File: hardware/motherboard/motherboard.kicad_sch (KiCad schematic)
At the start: 80 parts, among them J1 JST-VH, J2 USB C 2.0, J3 JST-VH, J4 JST-PH, J5 IMU Connector, Q1 TSM7P06CP_ROG, Q2 TSM7P06CP_ROG, SW10 B, SW11 X, SW12 Y, SW13 Start, SW14 Select, SW2 Reset, SW3 A, SW4 B, SW5 LB, SW6 RB, SW7 X, SW8 Y, SW9 A, U1 ESP32-S3-WROOM-1, U2 TPS75533KTTRG3, U3 TLV75709PDBV, U4 MCP73831-2-OT

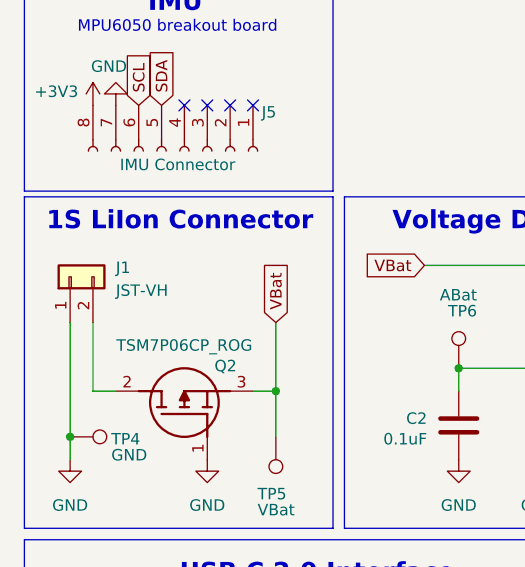
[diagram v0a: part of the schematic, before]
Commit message: Cont. Motherboard Layout
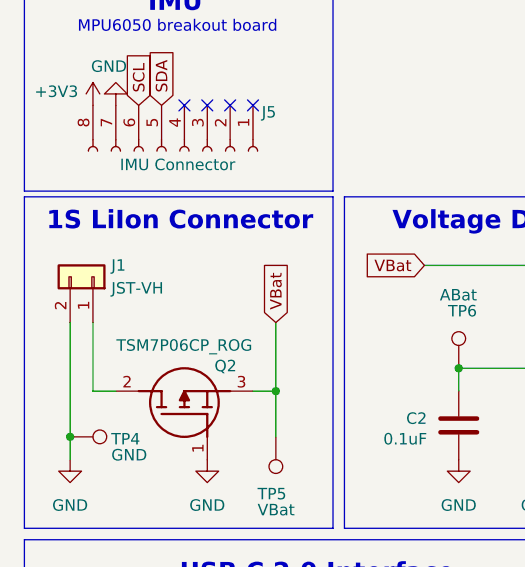
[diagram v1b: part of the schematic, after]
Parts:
- C1, C10, C5, C6, C7, C8: footprint (none) -> Capacitor_SMD:C_1206_3216Metric_Pad1.33x1.80mm_HandSolder
- C12, C13, C14, C15, C16, C17, C18, C19, C20, C21, C22, C23: footprint Capacitor_SMD:C_0201_0603Metric -> Capacitor_SMD:C_1206_3216Metric_Pad1.33x1.80mm_HandSolder
- C2, C4: footprint (none) -> Capacitor_SMD:C_0805_2012Metric_Pad1.18x1.45mm_HandSolder
- C3: footprint (none) -> Capacitor_Tantalum_SMD:CP_EIA-7343-31_Kemet-D
- R1, R10, R2, R23, R24, R25, R3, R4, R5, R6, R7, R9: footprint (none) -> Resistor_SMD:R_0805_2012Metric_Pad1.20x1.40mm_HandSolder
- R11, R12, R13, R14, R15, R16, R17, R18, R19, R20, R21, R22, R8: footprint Resistor_SMD:R_0603_1608Metric -> Resistor_SMD:R_0805_2012Metric_Pad1.20x1.40mm_HandSolder
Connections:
- net GND: now also J1.2 (Pin_2); no longer J1.1 (Pin_1)
- net at Q2.2 (D): now also J1.1 (Pin_1); no longer J1.2 (Pin_2)
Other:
- moved on the sheet: J1

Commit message: Routing 💀
Layout and routing. Used 3v3 plane to route some power traces.

Also added full size joystick model and footprint and schematic.
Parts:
- removed JY1: B10k, esp32_handheld:Low_Profile_Joystick, symbol esp32_handheld:Low_Profile_Joystick
- added C23: 1uF, Capacitor_SMD:C_0805_2012Metric_Pad1.18x1.45mm_HandSolder, symbol Device:C
- added R26: 10k, Resistor_SMD:R_0805_2012Metric_Pad1.20x1.40mm_HandSolder, symbol Device:R_US
- added U5: COM-09032, esp32_handheld:XDCR_COM-09032, symbol esp32_handheld:COM-09032
- C1: renamed from C12; footprint Capacitor_SMD:C_1206_3216Metric_Pad1.33x1.80mm_HandSolder -> Capacitor_SMD:C_0805_2012Metric_Pad1.18x1.45mm_HandSolder
- C10: renamed from C19; footprint Capacitor_SMD:C_1206_3216Metric_Pad1.33x1.80mm_HandSolder -> Capacitor_SMD:C_0805_2012Metric_Pad1.18x1.45mm_HandSolder
- C11: renamed from C20; footprint Capacitor_SMD:C_1206_3216Metric_Pad1.33x1.80mm_HandSolder -> Capacitor_SMD:C_0805_2012Metric_Pad1.18x1.45mm_HandSolder
- C12: renamed from C21; footprint Capacitor_SMD:C_1206_3216Metric_Pad1.33x1.80mm_HandSolder -> Capacitor_SMD:C_0805_2012Metric_Pad1.18x1.45mm_HandSolder
- C14: renamed from C10; footprint Capacitor_SMD:C_1206_3216Metric_Pad1.33x1.80mm_HandSolder -> Capacitor_SMD:C_0805_2012Metric_Pad1.18x1.45mm_HandSolder
- C15: renamed from C8; footprint Capacitor_SMD:C_1206_3216Metric_Pad1.33x1.80mm_HandSolder -> Capacitor_SMD:C_0805_2012Metric_Pad1.18x1.45mm_HandSolder
- C17: renamed from C7; footprint Capacitor_SMD:C_1206_3216Metric_Pad1.33x1.80mm_HandSolder -> Capacitor_SMD:C_0805_2012Metric_Pad1.18x1.45mm_HandSolder
- C18: renamed from C6; footprint Capacitor_SMD:C_1206_3216Metric_Pad1.33x1.80mm_HandSolder -> Capacitor_SMD:C_0805_2012Metric_Pad1.18x1.45mm_HandSolder
- C19: renamed from C1; footprint Capacitor_SMD:C_1206_3216Metric_Pad1.33x1.80mm_HandSolder -> Capacitor_SMD:C_0805_2012Metric_Pad1.18x1.45mm_HandSolder
- C2: renamed from C13; footprint Capacitor_SMD:C_1206_3216Metric_Pad1.33x1.80mm_HandSolder -> Capacitor_SMD:C_0805_2012Metric_Pad1.18x1.45mm_HandSolder
- C21: renamed from C5; footprint Capacitor_SMD:C_1206_3216Metric_Pad1.33x1.80mm_HandSolder -> Capacitor_SMD:C_0805_2012Metric_Pad1.18x1.45mm_HandSolder
- C22: renamed from C11; footprint (none) -> Capacitor_SMD:C_0805_2012Metric_Pad1.18x1.45mm_HandSolder
- C3: renamed from C16; footprint Capacitor_SMD:C_1206_3216Metric_Pad1.33x1.80mm_HandSolder -> Capacitor_SMD:C_0805_2012Metric_Pad1.18x1.45mm_HandSolder
- C4: renamed from C17; footprint Capacitor_SMD:C_1206_3216Metric_Pad1.33x1.80mm_HandSolder -> Capacitor_SMD:C_0805_2012Metric_Pad1.18x1.45mm_HandSolder
- C5: renamed from C14; footprint Capacitor_SMD:C_1206_3216Metric_Pad1.33x1.80mm_HandSolder -> Capacitor_SMD:C_0805_2012Metric_Pad1.18x1.45mm_HandSolder
- C6: renamed from C15; footprint Capacitor_SMD:C_1206_3216Metric_Pad1.33x1.80mm_HandSolder -> Capacitor_SMD:C_0805_2012Metric_Pad1.18x1.45mm_HandSolder
- C7: renamed from C22; footprint Capacitor_SMD:C_1206_3216Metric_Pad1.33x1.80mm_HandSolder -> Capacitor_SMD:C_0805_2012Metric_Pad1.18x1.45mm_HandSolder
- C8: renamed from C23; footprint Capacitor_SMD:C_1206_3216Metric_Pad1.33x1.80mm_HandSolder -> Capacitor_SMD:C_0805_2012Metric_Pad1.18x1.45mm_HandSolder
- C9: renamed from C18; footprint Capacitor_SMD:C_1206_3216Metric_Pad1.33x1.80mm_HandSolder -> Capacitor_SMD:C_0805_2012Metric_Pad1.18x1.45mm_HandSolder
- SW1: renamed from SW3; footprint (none) -> Button_Switch_THT:SW_PUSH_6mm
- SW10: value B -> Right; footprint (none) -> Button_Switch_THT:SW_PUSH_6mm
- SW11: value X -> Left; footprint (none) -> Button_Switch_THT:SW_PUSH_6mm
- SW12: value Y -> Up; footprint (none) -> Button_Switch_THT:SW_PUSH_6mm
- SW2: renamed from SW4; footprint (none) -> Button_Switch_THT:SW_PUSH_6mm
- SW3: renamed from SW7; footprint (none) -> Button_Switch_THT:SW_PUSH_6mm
- SW4: renamed from SW8; footprint (none) -> Button_Switch_THT:SW_PUSH_6mm
- SW7: renamed from SW13; footprint (none) -> Button_Switch_THT:SW_PUSH_6mm
- SW8: renamed from SW14; footprint (none) -> Button_Switch_THT:SW_PUSH_6mm
- SW9: value A -> Down; footprint (none) -> Button_Switch_THT:SW_PUSH_6mm
- renumbered C2 to C13, C3 to C16, C4 to C20, D2 to D1, D1 to D2, J5 to J1, J1 to J2, J2 to J5, Q2 to Q1, Q1 to Q2, R11 to R1, R18 to R10, R19 to R11, R20 to R12, R5 to R13, R8 to R14, R9 to R15, R10 to R16, R24 to R17, R6 to R18, R23 to R19, R12 to R2, R25 to R20, R7 to R21, R2 to R22, R3 to R23, R4 to R24, R1 to R25, R15 to R3, R16 to R4, R13 to R5, R14 to R6, R21 to R7, R22 to R8, R17 to R9, SW2 to SW13, TP6 to TP1, TP4 to TP2, TP5 to TP3, TP2 to TP4, TP1 to TP5, TP3 to TP6, U4 to U2, U2 to U3, U3 to U4
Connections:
- net +3V3: now also R26.1, U5.H1 (H+), U5.V1 (V+)
- net AX: now also U5.H2 (H)
- net AY: now also U5.V2 (V)
- net GND: now also C23.2, U5.B2A (SEL-), U5.H3 (H-), U5.S1 (SHIELD), U5.S2 (SHIELD__1), U5.S3 (SHIELD__2), U5.S4 (SHIELD__3), U5.V3 (V-)
- new net StckBtn: C23.1, R26.2, U5.B1A (SEL+)

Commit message: Will Notes
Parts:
- R21: value ??? -> 2k
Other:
- note removed: "Confirm charge programing resistance"
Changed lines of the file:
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@@
 		)
 	)
-	(text "Confirm charge\nprograming\nresistance"
-		(exclude_from_sim no)
-		(at 85.344 146.812 0)
-		(effects
-			(font
-				(size 0.762 0.762)
-				(thickness 0.0953)
-			)
-			(justify left)
-		)
-	)
 	(text "IMU"
 		(exclude_from_sim no)
@@
 		(at 30.48 102.87)
 	)
-	(bus_entry
-		(at 144.78 100.33)
-		(size 2.54 2.54)
-		(stroke
-			(width 0)
-			(type default)
-		)
-	)
 	(wire
 		(pts
@@
 	(global_label "StckBtn"
 		(shape input)
-		(at 278.13 41.91 180)
+		(at 271.78 22.86 180)
 		(fields_autoplaced yes)
 		(effects
@@
 		)
 		(property "Intersheetrefs" "${INTERSHEET_REFS}"
-			(at 267.9482 41.91 0)
+			(at 261.5982 22.86 0)
 			(effects
 				(font
@@
 			)
 		)
-		(property "Value" "???"
+		(property "Value" "2k"
 			(at 91.186 143.256 90)
 			(effects

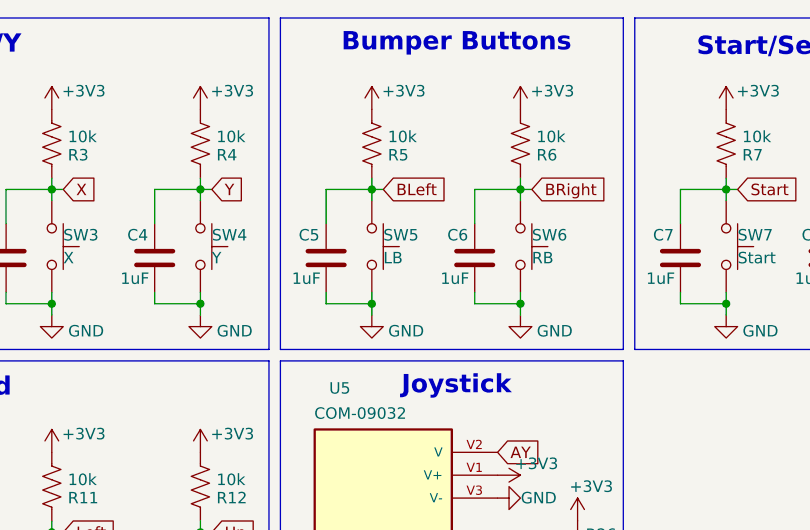
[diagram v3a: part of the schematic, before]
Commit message: Added bumper buttons
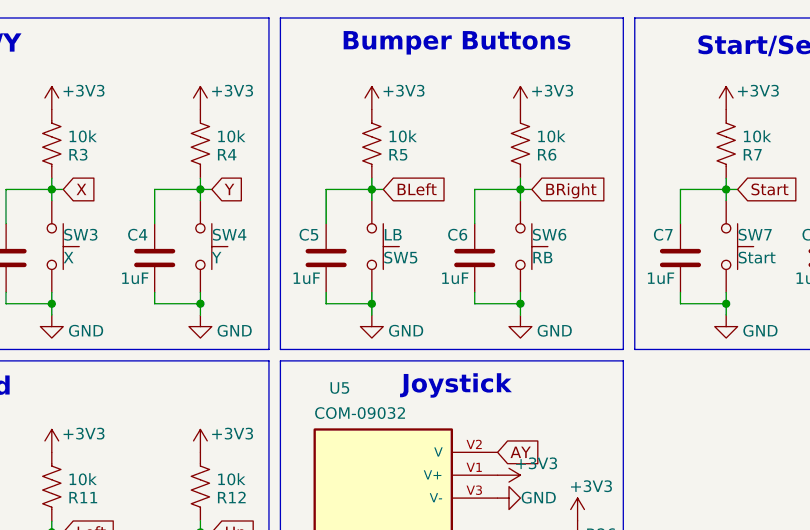
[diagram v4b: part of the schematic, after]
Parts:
- SW5, SW6: footprint (none) -> Button_Switch_THT:SW_Tactile_SPST_Angled_PTS645Vx58-2LFS
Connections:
- net BLeft: now also SW5.2; no longer SW5.1
- net GND: now also SW5.1; no longer SW5.2
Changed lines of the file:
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@@
 			)
 		)
-		(property "Footprint" ""
+		(property "Footprint" "Button_Switch_THT:SW_Tactile_SPST_Angled_PTS645Vx58-2LFS"
 			(at 113.03 38.1 0)
 			(effects
@@
 		(lib_id "Switch:SW_Push")
 		(at 91.44 38.1 270)
+		(mirror x)
 		(unit 1)
 		(exclude_from_sim no)
@@
 		(dnp no)
 		(property "Reference" "SW5"
+			(at 92.71 39.37 90)
+			(effects
+				(font
+					(size 1.27 1.27)
+				)
+				(justify left)
+			)
+		)
+		(property "Value" "LB"
 			(at 92.71 36.83 90)
 			(effects
@@
 			)
 		)
-		(property "Value" "LB"
-			(at 92.71 39.37 90)
-			(effects
-				(font
-					(size 1.27 1.27)
-				)
-				(justify left)
-			)
-		)
-		(property "Footprint" ""
+		(property "Footprint" "Button_Switch_THT:SW_Tactile_SPST_Angled_PTS645Vx58-2LFS"
 			(at 96.52 38.1 0)
 			(effects

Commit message: Reset Button
SMD Reset button on back behind MCU
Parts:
- SW13: footprint (none) -> Button_Switch_SMD:SW_SPST_CK_RS282G05A3
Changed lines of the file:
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@@
 			)
 		)
-		(property "Footprint" ""
+		(property "Footprint" "Button_Switch_SMD:SW_SPST_CK_RS282G05A3"
 			(at 132.08 137.16 0)
 			(effects

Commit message: Right Side Controls Routing
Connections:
- net B: now also U1.34 (IO41); no longer U1.33 (IO40)
- net BRight: now also U1.31 (IO38)
- net X: now also U1.33 (IO40); no longer U1.34 (IO41)
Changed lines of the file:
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@@
-	(wire
-		(pts
-			(xy 237.49 55.88) (xy 246.38 55.88)
-		)
-		(stroke
-			(width 0)
-			(type default)
-		)
-	)
 	(wire
 		(pts
@@
 	(global_label "BRight"
 		(shape input)
-		(at 266.7 44.45 180)
-		(fields_autoplaced yes)
-		(effects
-			(font
-				(size 1.27 1.27)
-			)
-			(justify right)
-		)
-		(property "Intersheetrefs" "${INTERSHEET_REFS}"
-			(at 257.5463 44.45 0)
-			(effects
-				(font
-					(size 1.27 1.27)
-				)
-				(justify right)
+		(at 237.49 55.88 0)
+		(fields_autoplaced yes)
+		(effects
+			(font
+				(size 1.27 1.27)
+			)
+			(justify left)
+		)
+		(property "Intersheetrefs" "${INTERSHEET_REFS}"
+			(at 246.6437 55.88 0)
+			(effects
+				(font
+					(size 1.27 1.27)
+				)
+				(justify left)
 				(hide yes)
 			)
@@
 	(global_label "B"
 		(shape input)
+		(at 237.49 63.5 0)
+		(fields_autoplaced yes)
+		(effects
+			(font
+				(size 1.27 1.27)
+			)
+			(justify left)
+		)
+		(property "Intersheetrefs" "${INTERSHEET_REFS}"
+			(at 241.7452 63.5 0)
+			(effects
+				(font
+					(size 1.27 1.27)
+				)
+				(justify left)
+				(hide yes)
+			)
+		)
+	)
+	(global_label "ACC1"
+		(shape input)
+		(at 147.32 133.35 0)
+		(fields_autoplaced yes)
+		(effects
+			(font
+				(size 1.27 1.27)
+			)
+			(justify left)
+		)
+		(property "Intersheetrefs" "${INTERSHEET_REFS}"
+			(at 155.1433 133.35 0)
+			(effects
+				(font
+					(size 1.27 1.27)
+				)
+				(justify left)
+				(hide yes)
+			)
+		)
+	)
+	(global_label "VPeripheral"
+		(shape input)
+		(at 226.06 143.51 180)
+		(fields_autoplaced yes)
+		(effects
+			(font
+				(size 1.27 1.27)
+			)
+			(justify right)
+		)
+		(property "Intersheetrefs" "${INTERSHEET_REFS}"
+			(at 212.2496 143.51 0)
+			(effects
+				(font
+					(size 1.27 1.27)
+				)
+				(justify right)
+				(hide yes)
+			)
+		)
+	)
+	(global_label "D+"
+		(shape input)
+		(at 66.04 163.83 0)
+		(fields_autoplaced yes)
+		(effects
+			(font
+				(size 1.27 1.27)
+			)
+			(justify left)
+		)
+		(property "Intersheetrefs" "${INTERSHEET_REFS}"
+			(at 71.8676 163.83 0)
+			(effects
+				(font
+					(size 1.27 1.27)
+				)
+				(justify left)
+				(hide yes)
+			)
+		)
+	)
+	(global_label "X"
+		(shape input)
 		(at 237.49 60.96 0)
 		(fields_autoplaced yes)
@@
 		)
 		(property "Intersheetrefs" "${INTERSHEET_REFS}"
-			(at 241.7452 60.96 0)
-			(effects
-				(font
-					(size 1.27 1.27)
-				)
-				(justify left)
-				(hide yes)
-			)
-		)
-	)
-	(global_label "ACC1"
-		(shape input)
-		(at 147.32 133.35 0)
-		(fields_autoplaced yes)
-		(effects
-			(font
-				(size 1.27 1.27)
-			)
-			(justify left)
-		)
-		(property "Intersheetrefs" "${INTERSHEET_REFS}"
-			(at 155.1433 133.35 0)
-			(effects
-				(font
-					(size 1.27 1.27)
-				)
-				(justify left)
-				(hide yes)
-			)
-		)
-	)
-	(global_label "VPeripheral"
-		(shape input)
-		(at 226.06 143.51 180)
-		(fields_autoplaced yes)
-		(effects
-			(font
-				(size 1.27 1.27)
-			)
-			(justify right)
-		)
-		(property "Intersheetrefs" "${INTERSHEET_REFS}"
-			(at 212.2496 143.51 0)
-			(effects
-				(font
-					(size 1.27 1.27)
-				)
-				(justify right)
-				(hide yes)
-			)
-		)
-	)
-	(global_label "D+"
-		(shape input)
-		(at 66.04 163.83 0)
-		(fields_autoplaced yes)
-		(effects
-			(font
-				(size 1.27 1.27)
-			)
-			(justify left)
-		)
-		(property "Intersheetrefs" "${INTERSHEET_REFS}"
-			(at 71.8676 163.83 0)
-			(effects
-				(font
-					(size 1.27 1.27)
-				)
-				(justify left)
-				(hide yes)
-			)
-		)
-	)
-	(global_label "X"
-		(shape input)
-		(at 237.49 63.5 0)
-		(fields_autoplaced yes)
-		(effects
-			(font
-				(size 1.27 1.27)
-			)
-			(justify left)
-		)
-		(property "Intersheetrefs" "${INTERSHEET_REFS}"
-			(at 241.6847 63.5 0)
-			(effects
-				(font
+			(at 241.6847 60.96 0)
+			(effects
+				(font

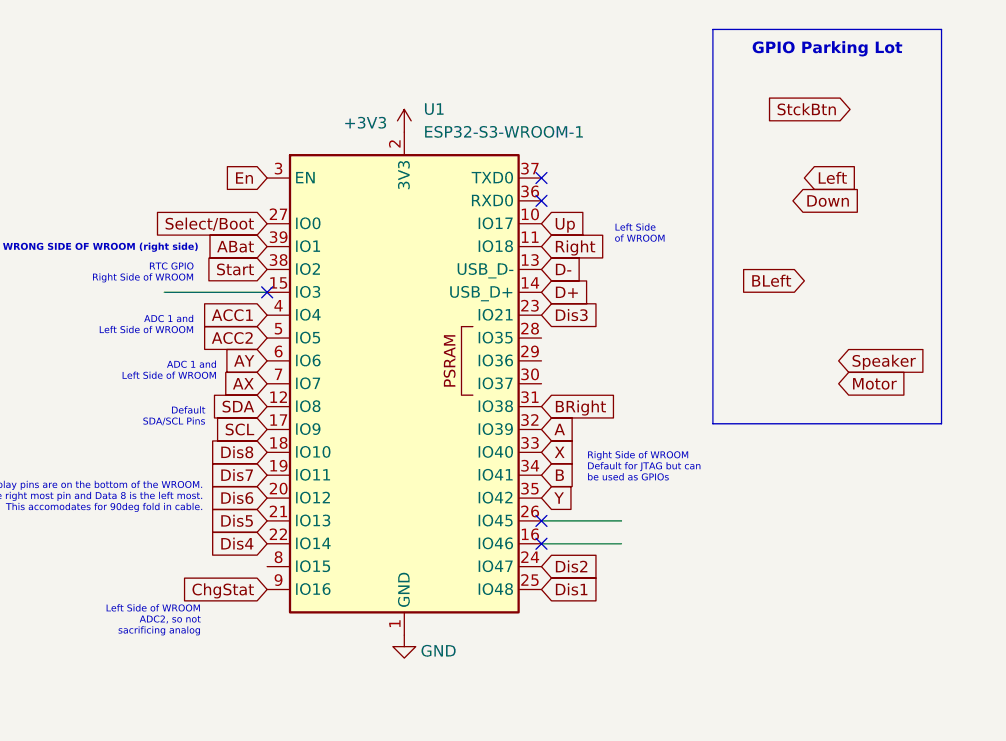
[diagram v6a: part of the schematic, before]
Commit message: Routed Joystick
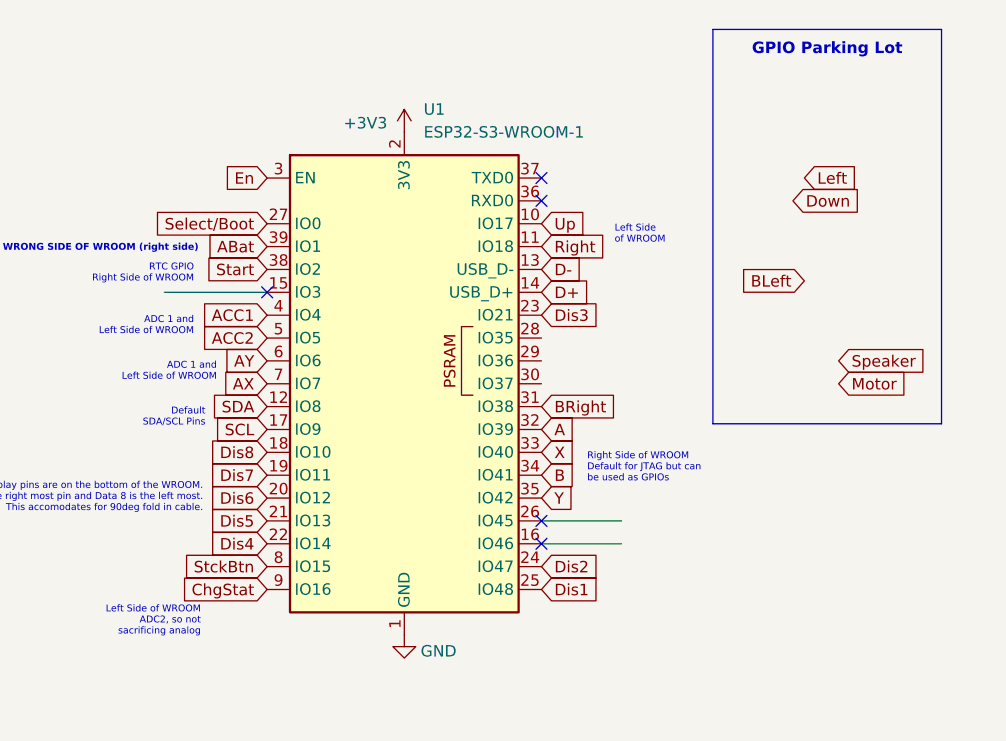
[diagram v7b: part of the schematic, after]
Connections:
- net StckBtn: now also U1.8 (IO15)
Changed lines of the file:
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@@
 	(global_label "StckBtn"
 		(shape input)
-		(at 271.78 22.86 180)
+		(at 207.01 73.66 180)
 		(fields_autoplaced yes)
 		(effects
@@
 		)
 		(property "Intersheetrefs" "${INTERSHEET_REFS}"
-			(at 261.5982 22.86 0)
+			(at 196.8282 73.66 0)
 			(effects
 				(font

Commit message: Updated gpios
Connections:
- net BLeft: now also U1.30 (IO37)
- net Down: now also U1.29 (IO36)
- net Left: now also U1.28 (IO35)
- net Motor: now also U1.16 (IO46)
- net Speaker: now also U1.26 (IO45)
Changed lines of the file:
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@@
 	(text "Needs motor speaker driver circuits"
 		(exclude_from_sim no)
-		(at 252.476 110.236 0)
+		(at 252.73 91.44 0)
 		(effects
 			(font
@@
 	(global_label "BLeft"
 		(shape input)
-		(at 266.7 41.91 180)
+		(at 237.49 53.34 0)
 		(fields_autoplaced yes)
 		(effects
@@
 				(size 1.27 1.27)
 			)
-			(justify right)
+			(justify left)
 		)
 		(property "Intersheetrefs" "${INTERSHEET_REFS}"
-			(at 258.8767 41.91 0)
+			(at 245.3133 53.34 0)
 			(effects
 				(font
 					(size 1.27 1.27)
 				)
-				(justify right)
+				(justify left)
 				(hide yes)
 			)
@@
 	(global_label "Left"
 		(shape input)
-		(at 266.7 30.48 0)
+		(at 237.49 48.26 0)
 		(fields_autoplaced yes)
 		(effects
@@
 		)
 		(property "Intersheetrefs" "${INTERSHEET_REFS}"
-			(at 273.2533 30.48 0)
+			(at 244.0433 48.26 0)
 			(effects
 				(font
@@
 	(global_label "Speaker"
 		(shape input)
-		(at 270.51 50.8 0)
+		(at 246.38 68.58 0)
 		(fields_autoplaced yes)
 		(effects
@@
 		)
 		(property "Intersheetrefs" "${INTERSHEET_REFS}"
-			(at 280.9942 50.8 0)
+			(at 256.8642 68.58 0)
 			(effects
 				(font
@@
 		)
 	)
+	(global_label "Motor"
+		(shape input)
+		(at 231.14 97.79 180)
+		(fields_autoplaced yes)
+		(effects
+			(font
+				(size 1.27 1.27)
+			)
+			(justify right)
+		)
+		(property "Intersheetrefs" "${INTERSHEET_REFS}"
+			(at 222.8935 97.79 0)
+			(effects
+				(font
+					(size 1.27 1.27)
+				)
+				(justify right)
+				(hide yes)
+			)
+		)
+	)
 	(global_label "Select{slash}Boot"
 		(shape input)
@@
 	(global_label "Down"
 		(shape input)
-		(at 265.43 33.02 0)
+		(at 237.49 50.8 0)
 		(fields_autoplaced yes)
 		(effects
@@
 		)
 		(property "Intersheetrefs" "${INTERSHEET_REFS}"
-			(at 273.3137 33.02 0)
+			(at 245.3737 50.8 0)
 			(effects
 				(font
@@
 	(global_label "Motor"
 		(shape input)
-		(at 270.51 53.34 0)
+		(at 246.38 71.12 0)
+		(fields_autoplaced yes)
+		(effects
+			(font
+				(size 1.27 1.27)
+			)
+			(justify left)
+		)
+		(property "Intersheetrefs" "${INTERSHEET_REFS}"
+			(at 254.6265 71.12 0)
+			(effects
+				(font
+					(size 1.27 1.27)
+				)
+				(justify left)
+				(hide yes)
+			)
+		)
+	)
+	(global_label "Speaker"
+		(shape input)
+		(at 271.78 97.79 0)
 		(fields_autoplaced yes)
 		(effects
@@
 		)
 		(property "Intersheetrefs" "${INTERSHEET_REFS}"
-			(at 278.7565 53.34 0)
+			(at 282.2642 97.79 0)
 			(effects
 				(font
